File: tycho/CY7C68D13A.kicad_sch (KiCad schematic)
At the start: 25 parts, among them U1 CY7C68013A-56LTX, U2 MIC5504-3.3YM5, U8 24LC128, Y1 24 MHz

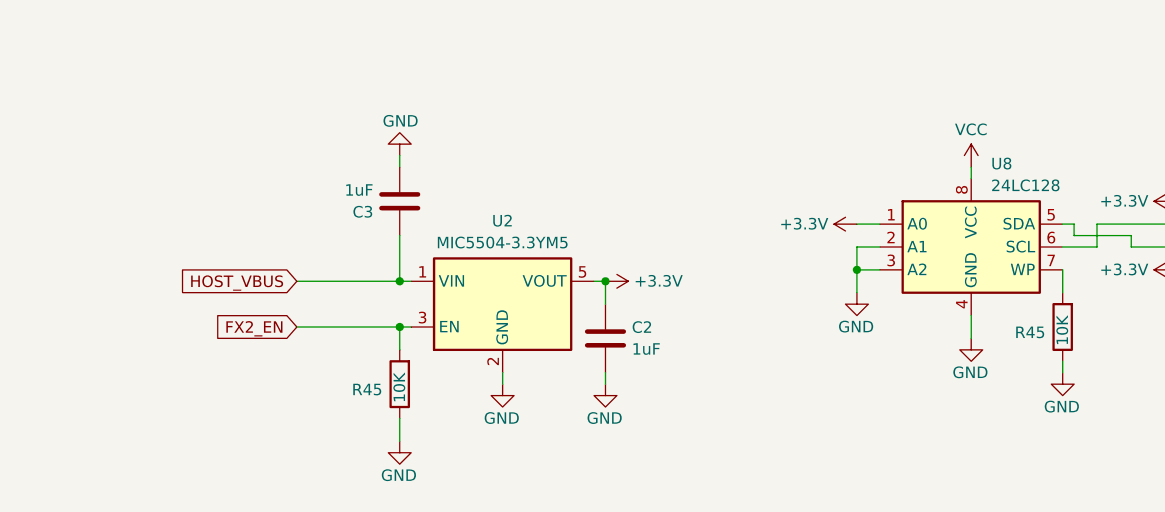
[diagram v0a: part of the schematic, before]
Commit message: Remove global labels and replace with hierarchical and standard labels
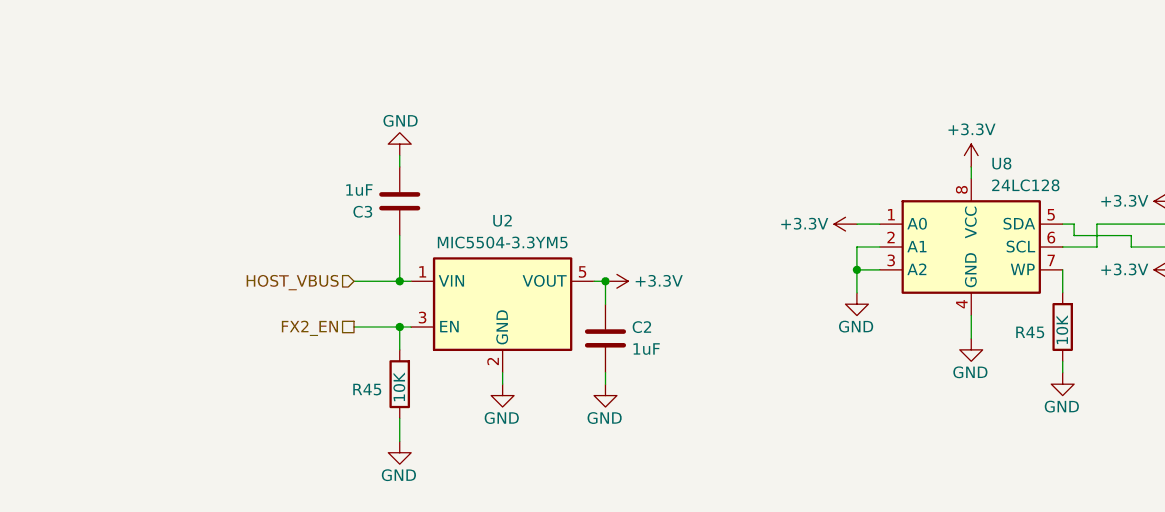
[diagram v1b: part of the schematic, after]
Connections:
- net VCC is gone; now on net +3.3V: U8.8 (VCC)
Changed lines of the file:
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@@
     (stroke (width 0) (type default))
   )
-  (wire (pts (xy 97.79 73.66) (xy 109.22 73.66))
+  (wire (pts (xy 104.14 73.66) (xy 109.22 73.66))
     (stroke (width 0) (type default))
   )
@@
     (stroke (width 0) (type default))
   )
-  (wire (pts (xy 97.79 68.58) (xy 109.22 68.58))
+  (wire (pts (xy 104.14 68.58) (xy 109.22 68.58))
     (stroke (width 0) (type default))
   )
@@
     (stroke (width 0) (type default))
   )
-  (global_label "FX2_EN" (shape input) (at 97.79 73.66 180) (fields_autoplaced)
+  (hierarchical_label "FX2_EN" (shape passive) (at 104.14 73.66 180) (fields_autoplaced)
     (effects (font (size 1.27 1.27)) (justify right))
-    (property "Intersheetrefs" "${INTERSHEET_REFS}" (at 87.8501 73.66 0)
-      (effects (font (size 1.27 1.27)) (justify right) hide)
-    )
-  )
-  (global_label "HOST_VBUS" (shape input) (at 97.79 68.58 180) (fields_autoplaced)
-    (effects (font (size 1.27 1.27)) (justify right))
-    (property "Intersheetrefs" "${INTERSHEET_REFS}" (at 84.1005 68.58 0)
-      (effects (font (size 1.27 1.27)) (justify right) hide)
-    )
   )
   (hierarchical_label "D_TA+" (shape passive) (at 207.01 85.09 180) (fields_autoplaced)
@@
   )
   (hierarchical_label "D_TA-" (shape passive) (at 207.01 82.55 180) (fields_autoplaced)
+    (effects (font (size 1.27 1.27)) (justify right))
+  )
+  (hierarchical_label "HOST_VBUS" (shape input) (at 104.14 68.58 180) (fields_autoplaced)
     (effects (font (size 1.27 1.27)) (justify right))
   )
@@
     )
   )
-  (symbol (lib_id "power:VCC") (at 172.72 55.88 0) (unit 1)
-    (in_bom yes) (on_board yes) (dnp no) (fields_autoplaced)
-    (property "Reference" "#PWR068" (at 172.72 59.69 0)
-      (effects (font (size 1.27 1.27)) hide)
-    )
-    (property "Value" "VCC" (at 172.72 51.7469 0)
-      (effects (font (size 1.27 1.27)))
-    )
-    (property "Footprint" "" (at 172.72 55.88 0)
-      (effects (font (size 1.27 1.27)) hide)
-    )
-    (property "Datasheet" "" (at 172.72 55.88 0)
-      (effects (font (size 1.27 1.27)) hide)
-    )
-    (pin "1")
-    (instances
-      (project "tycho"
-        (path "/4ed1cbaf-15e8-40e5-8366-86487d525fd5"
-          (reference "#PWR068") (unit 1)
-        )
-        (path "/4ed1cbaf-15e8-40e5-8366-86487d525fd5/b3c8fc2b-e9c9-4d47-a73a-55bc7ffe8734"
-          (reference "#PWR099") (unit 1)
-        )
-      )
-    )
-  )
   (symbol (lib_id "Device:C") (at 138.43 132.08 0) (unit 1)
     (in_bom yes) (on_board yes) (dnp no)
@@
         )
       )
+    )
+  )
+  (symbol (lib_id "power:+3.3V") (at 172.72 55.88 0) (unit 1)
+    (in_bom yes) (on_board yes) (dnp no) (fields_autoplaced)
+    (property "Reference" "#PWR088" (at 172.72 59.69 0)
+      (effects (font (size 1.27 1.27)) hide)
+    )
+    (property "Value" "+3.3V" (at 172.72 51.7469 0)
+      (effects (font (size 1.27 1.27)))
+    )
+    (property "Footprint" "" (at 172.72 55.88 0)
+      (effects (font (size 1.27 1.27)) hide)
+    )
+    (property "Datasheet" "" (at 172.72 55.88 0)
+      (effects (font (size 1.27 1.27)) hide)
+    )
+    (pin "1")
+    (instances
+      (project "tycho"
+        (path "/4ed1cbaf-15e8-40e5-8366-86487d525fd5/b3c8fc2b-e9c9-4d47-a73a-55bc7ffe8734"
+          (reference "#PWR088") (unit 1)
+        )
+      )

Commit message: Completed routing, reworked polygons, tidied up, passes DRC.
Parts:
- C41, C42: footprint Capacitor_SMD:C_1206_3216Metric_Pad1.33x1.80mm_HandSolder -> Capacitor_SMD:C_0402_1005Metric_Pad0.74x0.62mm_HandSolder; Manufacturer PSA(Prosperity Dielectrics) -> (none); Part Number FV31N120J102PXG -> (none)
- U1: footprint Package_DFN_QFN:QFN-56-1EP_8x8mm_P0.5mm_EP4.5x5.2mm_ThermalVias_TopTented -> tycho:QFN-56-1EP_8x8mm_P0.5mm_EP4.5x5.2mm_ThermalVias_TopTented
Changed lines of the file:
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@@
       (effects (font (size 1.27 1.27)) (justify left))
     )
-    (property "Footprint" "Package_DFN_QFN:QFN-56-1EP_8x8mm_P0.5mm_EP4.5x5.2mm_ThermalVias_TopTented" (at 228.6 33.02 0)
+    (property "Footprint" "tycho:QFN-56-1EP_8x8mm_P0.5mm_EP4.5x5.2mm_ThermalVias_TopTented" (at 228.6 33.02 0)
       (effects (font (size 1.27 1.27)) hide)
     )
@@
       (effects (font (size 1.27 1.27)) (justify left))
     )
-    (property "Footprint" "Capacitor_SMD:C_1206_3216Metric_Pad1.33x1.80mm_HandSolder" (at 173.6852 138.43 0)
+    (property "Footprint" "Capacitor_SMD:C_0402_1005Metric_Pad0.74x0.62mm_HandSolder" (at 173.6852 138.43 0)
       (effects (font (size 1.27 1.27)) hide)
     )
@@
       (effects (font (size 1.27 1.27)) hide)
     )
-    (property "Manufacturer" "PSA(Prosperity Dielectrics)" (at 172.72 134.62 0)
+    (property "Manufacturer" "" (at 172.72 134.62 0)
       (effects (font (size 1.27 1.27)) hide)
     )
-    (property "Part Number" "FV31N120J102PXG" (at 172.72 134.62 0)
+    (property "Part Number" "" (at 172.72 134.62 0)
       (effects (font (size 1.27 1.27)) hide)
     )
-    (property "Description" "1kV 12pF C0G ±5% 1206  Multilayer Ceramic Capacitors MLCC - SMD/SMT ROHS" (at 172.72 134.62 0)
+    (property "Description" "" (at 172.72 134.62 0)
       (effects (font (size 1.27 1.27)) hide)
     )
@@
       (effects (font (size 1.27 1.27)) (justify left))
     )
-    (property "Footprint" "Capacitor_SMD:C_1206_3216Metric_Pad1.33x1.80mm_HandSolder" (at 190.1952 138.43 0)
+    (property "Footprint" "Capacitor_SMD:C_0402_1005Metric_Pad0.74x0.62mm_HandSolder" (at 190.1952 138.43 0)
       (effects (font (size 1.27 1.27)) hide)
     )
@@
       (effects (font (size 1.27 1.27)) hide)
     )
-    (property "Manufacturer" "PSA(Prosperity Dielectrics)" (at 189.23 134.62 0)
+    (property "Manufacturer" "" (at 189.23 134.62 0)
       (effects (font (size 1.27 1.27)) hide)
     )
-    (property "Part Number" "FV31N120J102PXG" (at 189.23 134.62 0)
+    (property "Part Number" "" (at 189.23 134.62 0)
       (effects (font (size 1.27 1.27)) hide)
     )
-    (property "Description" "1kV 12pF C0G ±5% 1206  Multilayer Ceramic Capacitors MLCC - SMD/SMT ROHS" (at 189.23 134.62 0)
+    (property "Description" "" (at 189.23 134.62 0)
       (effects (font (size 1.27 1.27)) hide)
     )

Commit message: add part numbers
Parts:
- C41, C42: Manufacturer (none) -> Murata Electronics; Part Number (none) -> GCQ1555C1H120GB01D
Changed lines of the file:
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@@
       (effects (font (size 1.27 1.27)) hide)
     )
-    (property "Manufacturer" "" (at 172.72 134.62 0)
+    (property "Manufacturer" "Murata Electronics" (at 172.72 134.62 0)
       (effects (font (size 1.27 1.27)) hide)
     )
-    (property "Part Number" "" (at 172.72 134.62 0)
+    (property "Part Number" "GCQ1555C1H120GB01D" (at 172.72 134.62 0)
       (effects (font (size 1.27 1.27)) hide)
     )
-    (property "Description" "" (at 172.72 134.62 0)
+    (property "Description" "CAP CER 12PF 50V C0G/NP0 0402" (at 172.72 134.62 0)
       (effects (font (size 1.27 1.27)) hide)
     )
@@
       (effects (font (size 1.27 1.27)) hide)
     )
-    (property "Manufacturer" "" (at 189.23 134.62 0)
+    (property "Manufacturer" "Murata Electronics" (at 189.23 134.62 0)
       (effects (font (size 1.27 1.27)) hide)
     )
-    (property "Part Number" "" (at 189.23 134.62 0)
+    (property "Part Number" "GCQ1555C1H120GB01D" (at 189.23 134.62 0)
       (effects (font (size 1.27 1.27)) hide)
     )
-    (property "Description" "" (at 189.23 134.62 0)
+    (property "Description" "CAP CER 12PF 50V C0G/NP0 0402" (at 189.23 134.62 0)
       (effects (font (size 1.27 1.27)) hide)
     )

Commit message: Update revision number, metadata, and schematic page numbers
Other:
- company: (none) -> Copyright 2023 Great Scott Gadgets
- title: (none) -> Tycho
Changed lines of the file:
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@@
 (kicad_sch (version 20230121) (generator eeschema)
   (paper "A4")
+  (title_block
+    (title "Tycho")
+    (date "${DATE}")
+    (rev "${VERSION}")
+    (company "Copyright 2023 Great Scott Gadgets")
+    (comment 1 "Licensed under the CERN-OHL-P v2")
+  )
   (junction (at 105.41 137.16) (diameter 0) (color 0 0 0 0)
   )

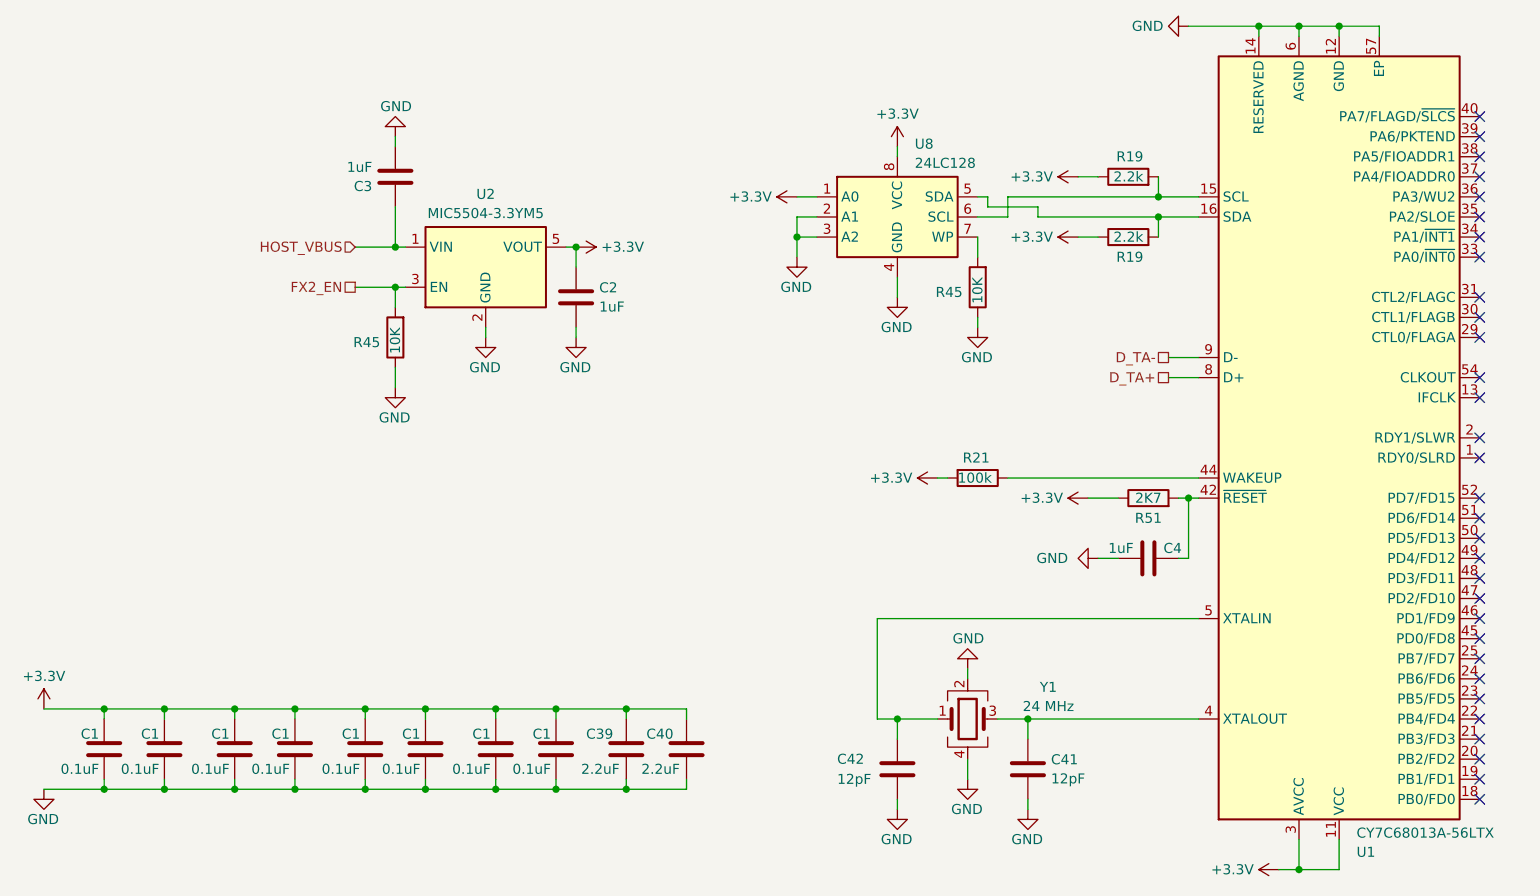
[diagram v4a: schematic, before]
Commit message: Change R65 to 22k
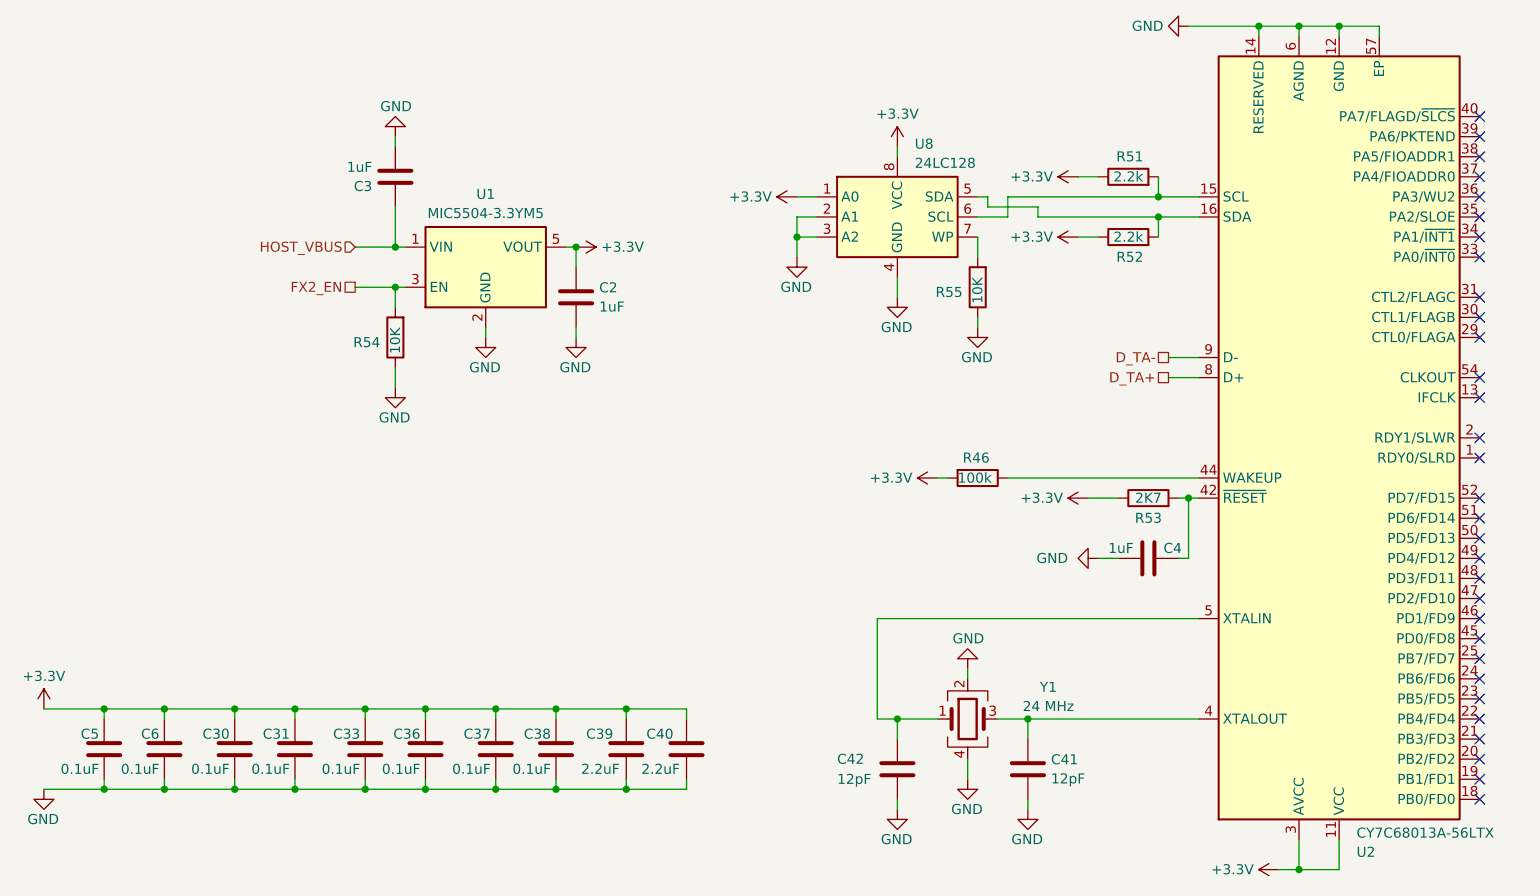
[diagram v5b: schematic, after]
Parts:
- renumbered C1 to C30, C1 to C31, C1 to C33, C1 to C36, C1 to C37, C1 to C38, C1 to C5, C1 to C6, R21 to R46, R19 to R51, R19 to R52, R51 to R53, R45 to R54, R45 to R55, U2 to U1, U1 to U2
